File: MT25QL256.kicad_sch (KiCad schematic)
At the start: 3 parts, among them U3 W25Q32JVZP

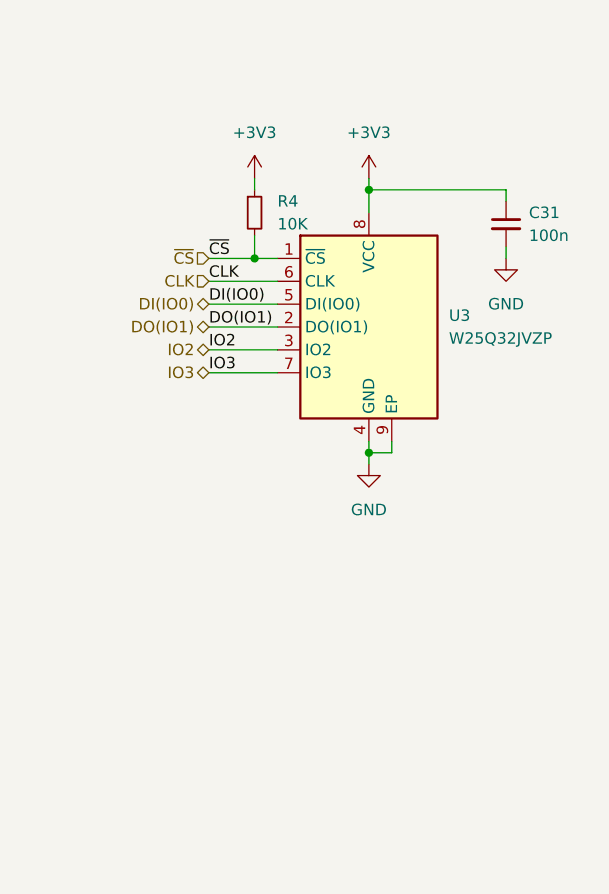
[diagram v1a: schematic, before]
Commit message: Finished SDRAM, QSPI FLASH (trace length not matched yet)
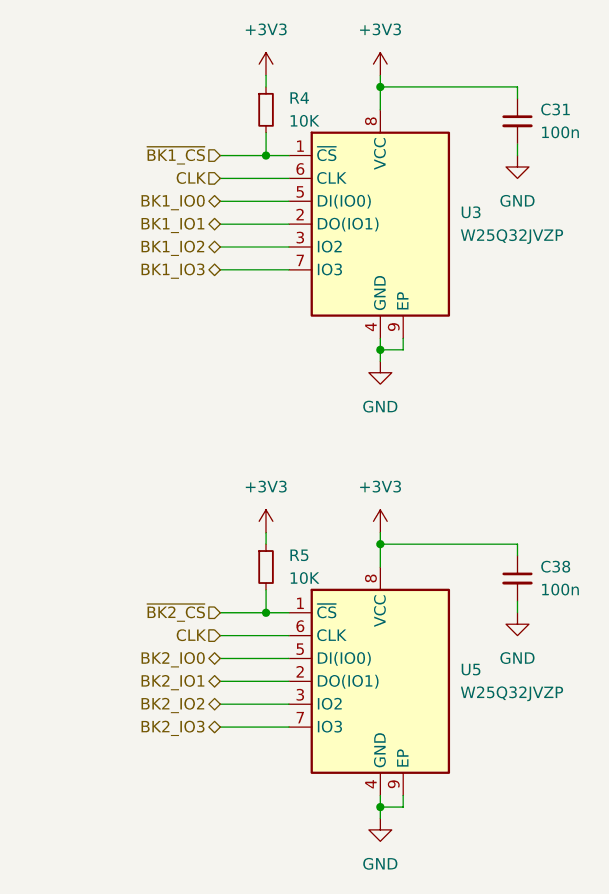
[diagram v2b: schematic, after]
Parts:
- added C38: 100n, Capacitor_SMD:C_0201_0603Metric, symbol Device:C_Small
- added R5: 10K, Resistor_SMD:R_0201_0603Metric, symbol Device:R_Small
- added U5: W25Q32JVZP, Package_SON:WSON-8-1EP_8x6mm_P1.27mm_EP3.4x4.3mm, symbol Memory_Flash:W25Q32JVZP
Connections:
- net +3V3: now also C38.1, R5.1, U5.8 (VCC)
- net CLK: now also U5.6 (CLK)
- net GND: now also C38.2, U5.4 (GND), U5.9 (EP)
- net DI(IO0) renamed BK1_IO0
- net DO(IO1) renamed BK1_IO1
- net IO2 renamed BK1_IO2
- net IO3 renamed BK1_IO3
- net ~{CS} renamed ~{BK1_CS}
- new net BK2_IO0: U5.5 (DI(IO0))
- new net BK2_IO1: U5.2 (DO(IO1))
- new net BK2_IO2: U5.3 (IO2)
- new net BK2_IO3: U5.7 (IO3)
- new net ~{BK2_CS}: R5.2, U5.1 (~{CS})
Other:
- moved on the sheet: C31, R4, U3

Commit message: 98% finished, st-link part left
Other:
- note added: "PB2"
- note added: "PB6"
- note added: "PC11"
- note added: "PF6"
- note added: "PF7"
- note added: "PF8"
- note added: "PF9"
- note added: "PG14"
- note added: "PG9"
- note added: "PH2"
- note added: "PH3"
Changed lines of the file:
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@@
+		)
+	)
+	(text "PB6"
+		(exclude_from_sim no)
+		(at 111.76 66.294 0)
+		(effects
+			(font
+				(size 1.27 1.27)
+			)
+		)
+	)
+	(text "PB2"
+		(exclude_from_sim no)
+		(at 111.76 119.634 0)
+		(effects
+			(font
+				(size 1.27 1.27)
+			)
+		)
+	)
+	(text "PF7"
+		(exclude_from_sim no)
+		(at 111.76 76.454 0)
+		(effects
+			(font
+				(size 1.27 1.27)
+			)
+		)
+	)
+	(text "PF8"
+		(exclude_from_sim no)
+		(at 111.76 71.374 0)
+		(effects
+			(font
+				(size 1.27 1.27)
+			)
+		)
+	)
+	(text "PG9"
+		(exclude_from_sim no)
+		(at 111.76 127.254 0)
+		(effects
+			(font
+				(size 1.27 1.27)
+			)
+		)
+	)
+	(text "PF6"
+		(exclude_from_sim no)
+		(at 111.76 78.994 0)
+		(effects
+			(font
+				(size 1.27 1.27)
+			)
+		)
+	)
+	(text "PG14"
+		(exclude_from_sim no)
+		(at 112.268 129.794 0)
+		(effects
+			(font
+				(size 1.27 1.27)
+			)
+		)
+	)
+	(text "PH3"
+		(exclude_from_sim no)
+		(at 111.76 124.714 0)
+		(effects
+			(font
+				(size 1.27 1.27)
+			)
+		)
+	)
+	(text "PC11"
+		(exclude_from_sim no)
+		(at 112.268 117.094 0)
+		(effects
+			(font
+				(size 1.27 1.27)
+			)
+		)
+	)
+	(text "PF9"
+		(exclude_from_sim no)
+		(at 111.76 73.914 0)
+		(effects
+			(font
+				(size 1.27 1.27)
+			)
+		)
+	)
+	(text "PH2"
+		(exclude_from_sim no)
+		(at 111.76 122.174 0)
+		(effects
+			(font
+				(size 1.27 1.27)
+			)
+		)
+	)
+	(text "PB2"
+		(exclude_from_sim no)
+		(at 111.76 68.834 0)
+		(effects
+			(font
+				(size 1.27 1.27)
+			)
 		)
 	)

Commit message: Adding JLCPCB Part #
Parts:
- C31, C38: JLCPCB Part # (none) -> C307380
- R4, R5: JLCPCB Part # (none) -> C473048
- U3, U5: JLCPCB Part # (none) -> C2986165
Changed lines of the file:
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@@
+			)
+		)
+		(property "JLCPCB Part #" "C307380"
+			(at 158.75 113.03 0)
+			(effects
+				(font
+					(size 1.27 1.27)
+				)
+				(hide yes)
 			)
 		)
@@
 			)
 		)
+		(property "JLCPCB Part #" "C2986165"
+			(at 143.51 124.46 0)
+			(effects
+				(font
+					(size 1.27 1.27)
+				)
+				(hide yes)
+			)
+		)
 		(pin "6"
 		)
@@
 			)
 		)
+		(property "JLCPCB Part #" "C473048"
+			(at 130.81 111.76 0)
+			(effects
+				(font
+					(size 1.27 1.27)
+				)
+				(hide yes)
+			)
+		)
 		(pin "2"
 		)
@@
 			)
 		)
+		(property "JLCPCB Part #" "C2986165"
+			(at 143.51 73.66 0)
+			(effects
+				(font
+					(size 1.27 1.27)
+				)
+				(hide yes)
+			)
+		)
 		(pin "6"
 		)
@@
 			)
 		)
+		(property "JLCPCB Part #" "C473048"
+			(at 130.81 60.96 0)
+			(effects
+				(font
+					(size 1.27 1.27)
+				)
+				(hide yes)
+			)
+		)
 		(pin "2"
 		)
@@
 			(at 158.75 62.23 0)
 			(effects
+				(font
+					(size 1.27 1.27)
+				)
+				(hide yes)
+			)
+		)
+		(property "JLCPCB Part #" "C307380"
+			(at 158.75 62.23 0)
+			(effects

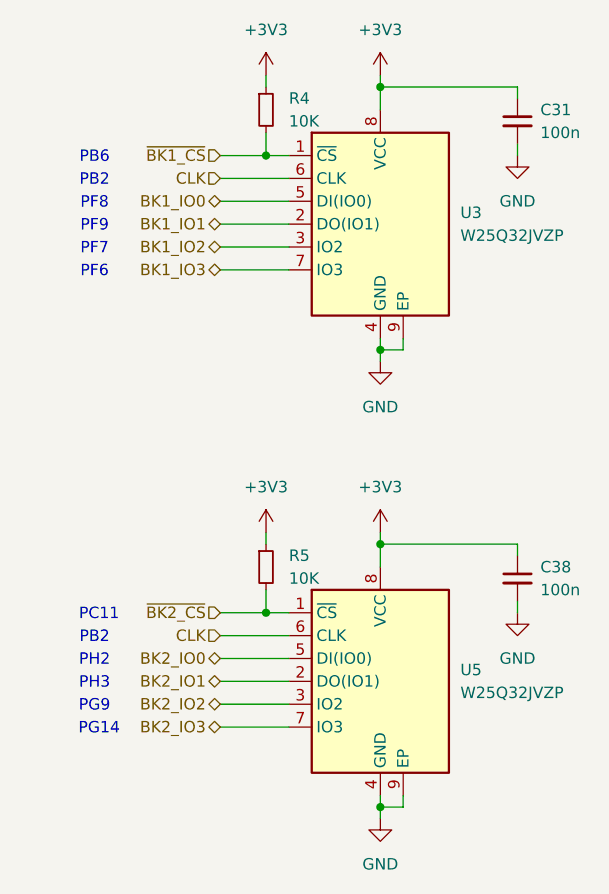
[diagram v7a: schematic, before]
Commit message: Finished LTDC tracks
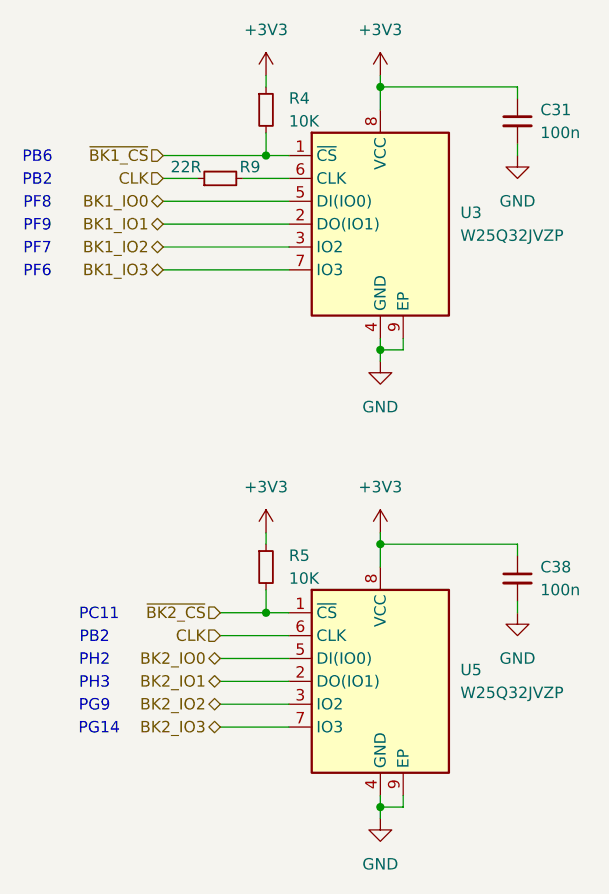
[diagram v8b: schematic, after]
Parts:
- added R9: 22R, Resistor_SMD:R_0201_0603Metric, symbol Device:R_Small
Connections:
- net CLK: now also R9.1; no longer U3.6 (CLK)
- new net: R9.2, U3.6 (CLK)
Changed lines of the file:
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@@
 	(text "PB6"
 		(exclude_from_sim no)
-		(at 111.76 66.294 0)
+		(at 105.41 66.294 0)
 		(effects
 			(font
@@
 	(text "PF7"
 		(exclude_from_sim no)
-		(at 111.76 76.454 0)
+		(at 105.41 76.454 0)
 		(effects
 			(font
@@
 	(text "PF8"
 		(exclude_from_sim no)
-		(at 111.76 71.374 0)
+		(at 105.41 71.374 0)
 		(effects
 			(font
@@
 	(text "PF6"
 		(exclude_from_sim no)
-		(at 111.76 78.994 0)
+		(at 105.41 78.994 0)
 		(effects
 			(font
@@
 	(text "PF9"
 		(exclude_from_sim no)
-		(at 111.76 73.914 0)
+		(at 105.41 73.914 0)
 		(effects
 			(font
@@
 	(text "PB2"
 		(exclude_from_sim no)
-		(at 111.76 68.834 0)
+		(at 105.41 68.834 0)
 		(effects
 			(font
@@
 	(wire
 		(pts
-			(xy 125.73 71.12) (xy 133.35 71.12)
+			(xy 119.38 71.12) (xy 133.35 71.12)
 		)
 		(stroke
@@
 	(wire
 		(pts
-			(xy 125.73 73.66) (xy 133.35 73.66)
+			(xy 119.38 73.66) (xy 133.35 73.66)
 		)
 		(stroke
@@
 	(wire
 		(pts
-			(xy 125.73 76.2) (xy 133.35 76.2)
+			(xy 119.38 76.2) (xy 133.35 76.2)
 		)
 		(stroke
@@
 	(wire
 		(pts
+			(xy 119.38 68.58) (xy 123.19 68.58)
+		)
+		(stroke
+			(width 0)
+			(type default)
+		)
+	)
+	(wire
+		(pts
 			(xy 130.81 57.15) (xy 130.81 58.42)
 		)
@@
 	(wire
 		(pts
-			(xy 125.73 78.74) (xy 133.35 78.74)
-		)
-		(stroke
-			(width 0)
-			(type default)
-		)
-	)
-	(wire
-		(pts
-			(xy 125.73 68.58) (xy 133.35 68.58)
+			(xy 119.38 78.74) (xy 133.35 78.74)
 		)
 		(stroke
@@
 	(wire
 		(pts
+			(xy 128.27 68.58) (xy 133.35 68.58)
+		)
+		(stroke
+			(width 0)
+			(type default)
+		)
+	)
+	(wire
+		(pts
 			(xy 143.51 139.7) (xy 143.51 138.43)
 		)
@@
 	(wire
 		(pts
-			(xy 125.73 66.04) (xy 130.81 66.04)
+			(xy 119.38 66.04) (xy 130.81 66.04)
 		)
 		(stroke
@@
 	(hierarchical_label "~{BK1_CS}"
 		(shape input)
-		(at 125.73 66.04 180)
+		(at 119.38 66.04 180)
 		(effects
 			(font
@@
 	(hierarchical_label "BK1_IO2"
 		(shape bidirectional)
-		(at 125.73 76.2 180)
+		(at 119.38 76.2 180)
 		(effects
 			(font
@@
 	(hierarchical_label "CLK"
 		(shape input)
-		(at 125.73 68.58 180)
+		(at 119.38 68.58 180)
 		(effects
 			(font
@@
 	(hierarchical_label "BK1_IO0"
 		(shape bidirectional)
-		(at 125.73 71.12 180)
+		(at 119.38 71.12 180)
 		(effects
 			(font
@@
 	(hierarchical_label "BK1_IO1"
 		(shape bidirectional)
-		(at 125.73 73.66 180)
+		(at 119.38 73.66 180)
 		(effects
 			(font
@@
 	(hierarchical_label "BK1_IO3"
 		(shape bidirectional)
-		(at 125.73 78.74 180)
+		(at 119.38 78.74 180)
 		(effects
 			(font
@@
 		(polyline
 			(pts
-				(xy 128.27 63.5) (xy 128.27 81.28) (xy 104.14 81.28) (xy 104.14 63.5)
+				(xy 129.54 62.23) (xy 129.54 80.01) (xy 102.87 80.01) (xy 102.87 62.23)
 			)
 			(stroke
@@
 		(length 2.54)
 		(shape round)
-		(at 115.57 63.5 0)
+		(at 116.84 62.23 0)
 		(fields_autoplaced yes)
 		(effects
@@
 		)
 		(property "Netclass" "QSPI_FLASH"
-			(at 116.2685 60.96 0)
+			(at 117.5385 59.69 0)
 			(effects
 				(font
@@
 		)
 		(property "Component Class" ""
-			(at -73.66 -8.89 0)
+			(at -72.39 -10.16 0)
 			(effects
 				(font
@@
 					(unit 1)
 				)
+			)
+		)
+	)
+	(symbol
+		(lib_id "Device:R_Small")
+		(at 125.73 68.58 90)
+		(unit 1)
+		(exclude_from_sim no)
+		(in_bom yes)
+		(on_board yes)
+		(dnp no)
+		(property "Reference" "R9"
+			(at 129.032 67.31 90)
+			(effects
+				(font
+					(size 1.27 1.27)
+				)
+			)
+		)
+		(property "Value" "22R"
+			(at 121.92 67.31 90)
+			(effects
+				(font
+					(size 1.27 1.27)
+				)
+			)
+		)
+		(property "Footprint" "Resistor_SMD:R_0201_0603Metric"
+			(at 125.73 68.58 0)
+			(effects
+				(font
+					(size 1.27 1.27)
+				)
+				(hide yes)
+			)
+		)
+		(property "Datasheet" "~"
+			(at 125.73 68.58 0)
+			(effects
+				(font
+					(size 1.27 1.27)
+				)
+				(hide yes)
+			)
+		)
+		(property "Description" "Resistor, small symbol"
+			(at 125.73 68.58 0)
+			(effects
+				(font
+					(size 1.27 1.27)
+				)
+				(hide yes)
+			)
+		)
+		(property "JLCPCB Part #" "C473048"
+			(at 125.73 68.58 0)
+			(effects
+				(font
+					(size 1.27 1.27)
+				)
+				(hide yes)
+			)
+		)
+		(pin "2"
+		)
+		(pin "1"
+		)
+		(instances
+			(project "siplex-som-s16"
+				(path "/3553d318-c74b-41b3-86db-bdd251e8121d/b2a8b37b-96db-4567-b891-31d7f85c3367"
+					(reference "R9")
+					(unit 1)
+				)
